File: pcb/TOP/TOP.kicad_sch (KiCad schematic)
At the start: 93 parts, among them J1 Conn_01x04, U1 ICL7660, U2 L78L15_SOT89, U3 TL074, U4 OPA2604

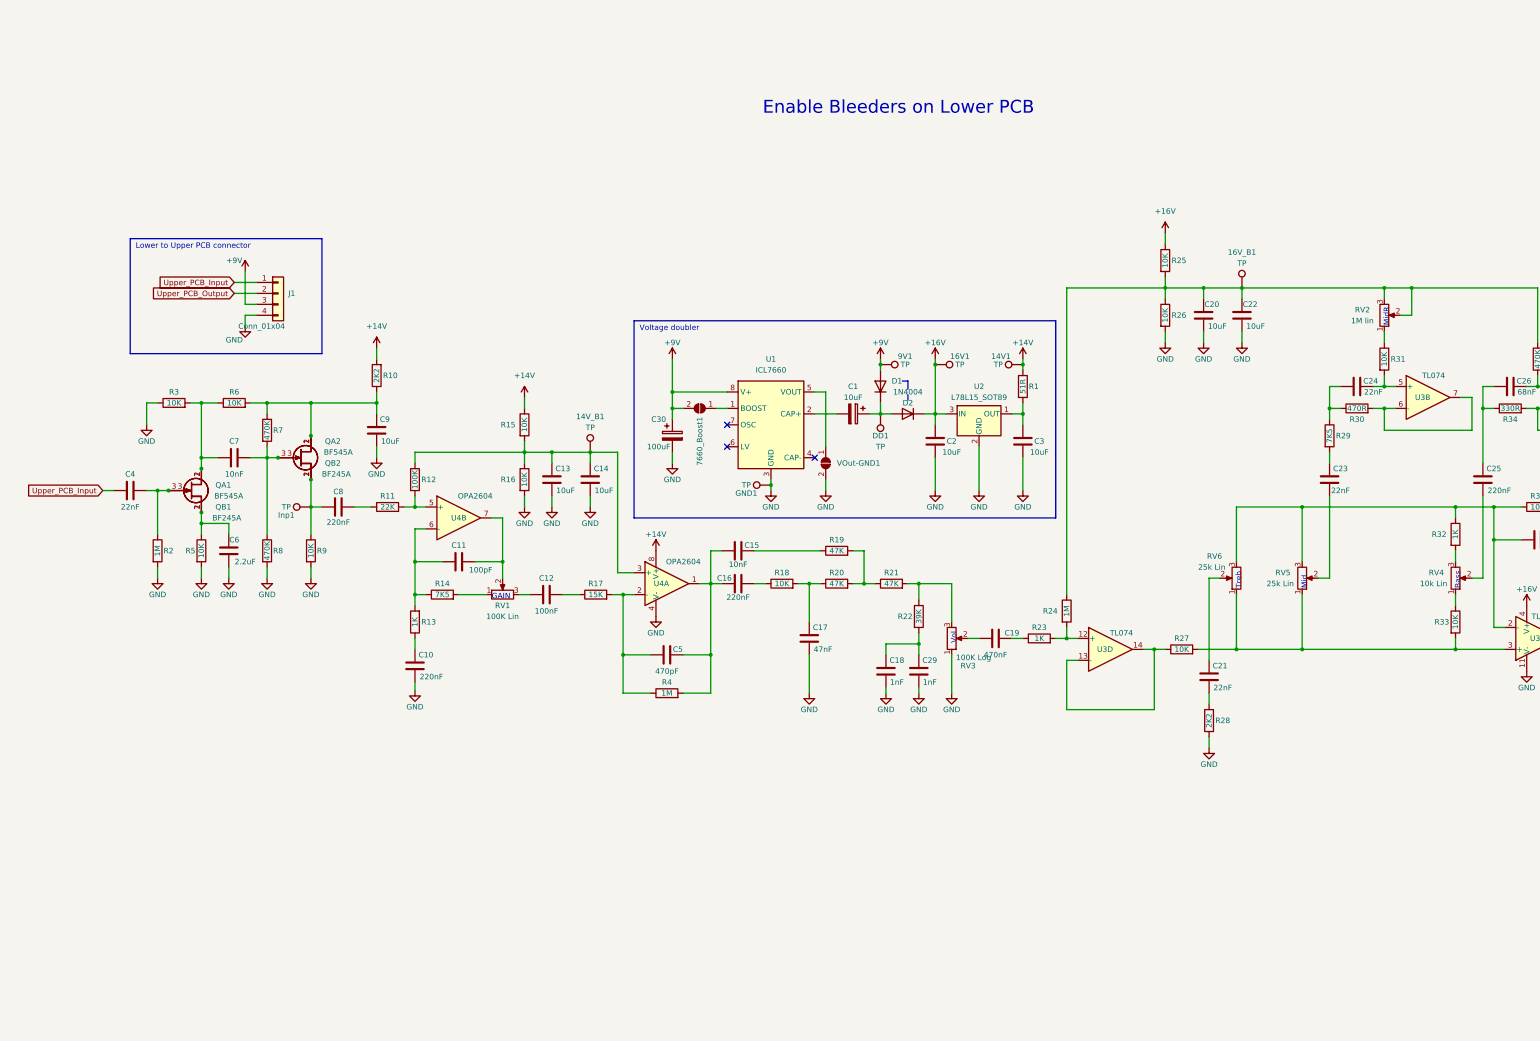
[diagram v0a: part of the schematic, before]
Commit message: [TOP] Fix 7660 -> 7660S in schematic; Make circuit fit for simulation of input stage
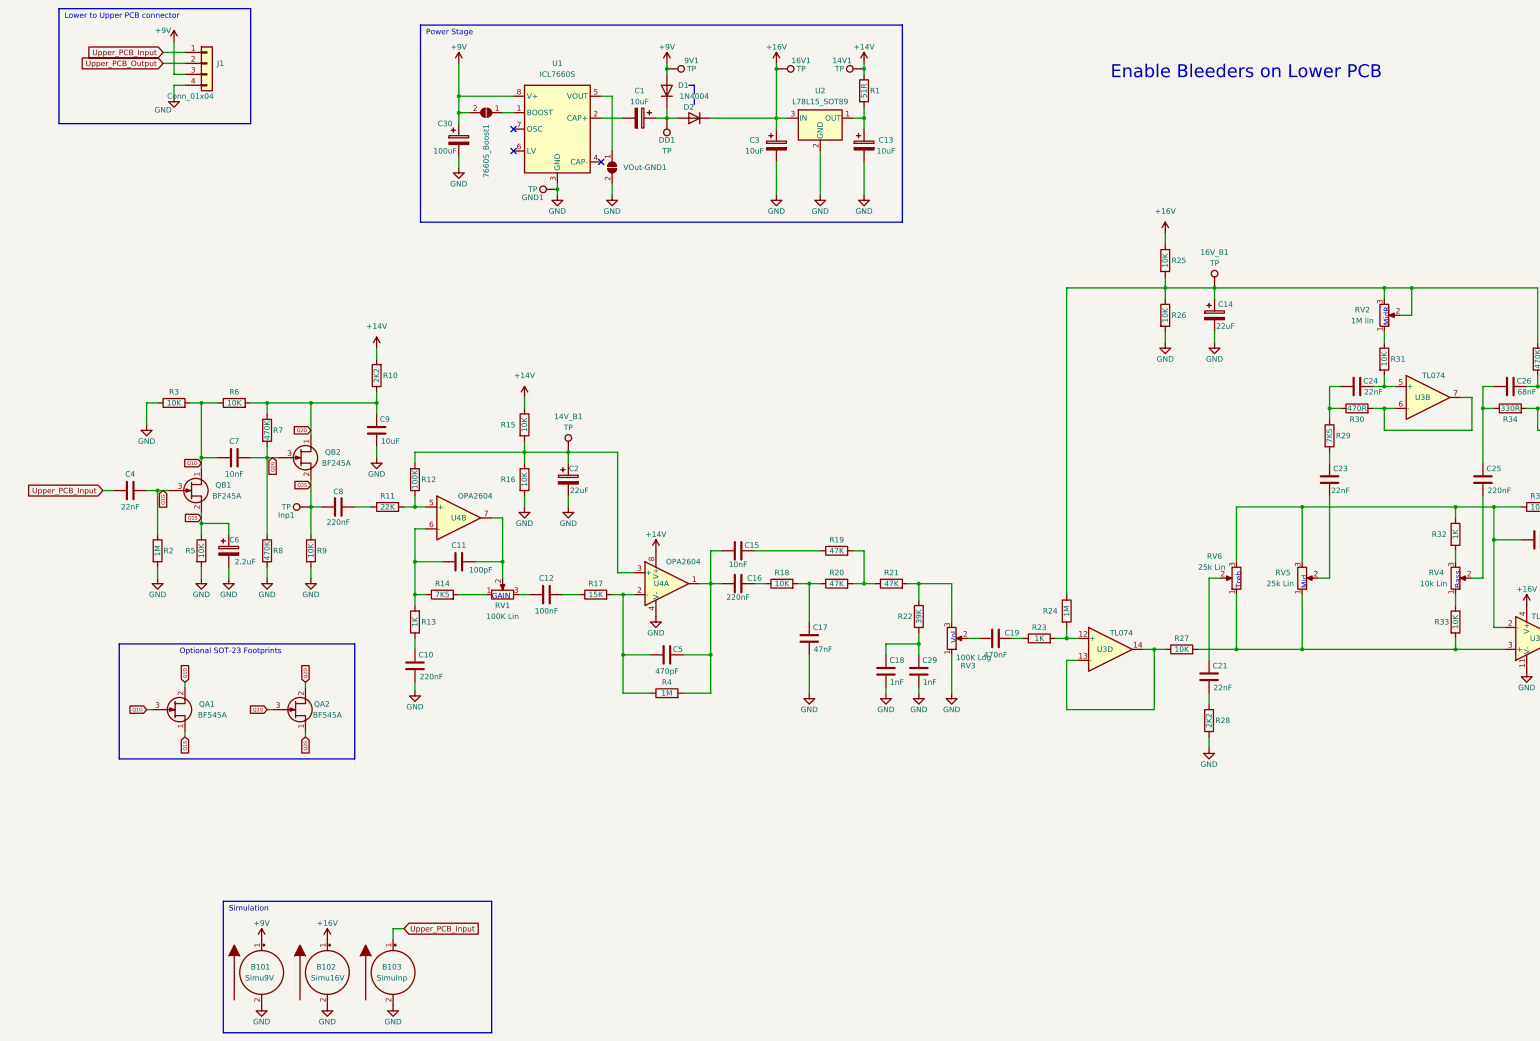
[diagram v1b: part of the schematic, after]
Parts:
- removed C13, C14, C2, C20, C22, C3: 10uF, Capacitor_SMD:C_0805_2012Metric, symbol Device:C
- removed C6: 2.2uF, Capacitor_SMD:C_0603_1608Metric, symbol Device:C
- added B101: Simu9V, symbol pspice:BSOURCE
- added B102: Simu16V, symbol pspice:BSOURCE
- added B103: SimuInp, symbol pspice:BSOURCE
- added C13, C3: 10uF, Capacitor_SMD:CP_Elec_4x5.4, symbol Device:C_Polarized
- added C14, C2: 22uF, symbol Device:C_Polarized
- added C6: 2.2uF, symbol Device:C_Polarized
- 14V1, 14V_B1, 16V1, 16V_B1, 9V1, DD1, GND1, Inp1, J1, RV1, RV2, RV3, RV4, RV5, RV6, U4, VOut-GND1: Spice_Netlist_Enabled (none) -> N
- 7660S_Boost1: renamed from 7660_Boost1; Spice_Netlist_Enabled (none) -> N
- C1, C9: Spice_Model (none) -> 10u; Spice_Netlist_Enabled (none) -> Y; Spice_Primitive (none) -> C
- C10, C16, C25, C8: Spice_Model (none) -> 220n; Spice_Netlist_Enabled (none) -> Y; Spice_Primitive (none) -> C
- C11: Spice_Model (none) -> 100p; Spice_Netlist_Enabled (none) -> Y; Spice_Primitive (none) -> C
- C12: Spice_Model (none) -> 100n; Spice_Netlist_Enabled (none) -> Y; Spice_Primitive (none) -> C
- C15, C7: Spice_Model (none) -> 10n; Spice_Netlist_Enabled (none) -> Y; Spice_Primitive (none) -> C
- C17: Spice_Model (none) -> 47n; Spice_Netlist_Enabled (none) -> Y; Spice_Primitive (none) -> C
- C18, C27, C29: Spice_Model (none) -> 1n; Spice_Netlist_Enabled (none) -> Y; Spice_Primitive (none) -> C
- C19, C28: Spice_Model (none) -> 470n; Spice_Netlist_Enabled (none) -> Y; Spice_Primitive (none) -> C
- C21, C23, C24, C4: Spice_Model (none) -> 22n; Spice_Netlist_Enabled (none) -> Y; Spice_Primitive (none) -> C
- C26: Spice_Model (none) -> 68n; Spice_Netlist_Enabled (none) -> Y; Spice_Primitive (none) -> C
- C30: Spice_Model (none) -> 100u; Spice_Netlist_Enabled (none) -> Y; Spice_Primitive (none) -> C
- C5: Spice_Model (none) -> 470p; Spice_Netlist_Enabled (none) -> Y; Spice_Primitive (none) -> C
- D1, D2: Spice_Lib_File (none) -> /home/chrismettal/mnt/Raidstone/Projects/_KiCAD_libraries_/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; Spice_Model (none) -> D1N4001; Spice_Netlist_Enabled (none) -> Y; Spice_Primitive (none) -> D
- QA1, QA2: Spice_Model (none) -> BF545A; Spice_Netlist_Enabled (none) -> N; Spice_Primitive (none) -> Q
- QB1, QB2: Spice_Lib_File (none) -> /home/chrismettal/mnt/Raidstone/Projects/_KiCAD_libraries_/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; Spice_Model (none) -> BF245A; Spice_Netlist_Enabled (none) -> Y; Spice_Node_Sequence (none) -> 1 3 2; Spice_Primitive (none) -> J
- R1: Spice_Model (none) -> 51; Spice_Netlist_Enabled (none) -> Y; Spice_Primitive (none) -> R
- R10, R28: Spice_Model (none) -> 2.2k; Spice_Netlist_Enabled (none) -> Y; Spice_Primitive (none) -> R
- R11: Spice_Model (none) -> 22k; Spice_Netlist_Enabled (none) -> Y; Spice_Primitive (none) -> R
- R12: Spice_Model (none) -> 100k; Spice_Netlist_Enabled (none) -> Y; Spice_Primitive (none) -> R
- R13, R23, R32: Spice_Model (none) -> 1k; Spice_Netlist_Enabled (none) -> Y; Spice_Primitive (none) -> R
- R14, R29: Spice_Model (none) -> 7.5k; Spice_Netlist_Enabled (none) -> Y; Spice_Primitive (none) -> R
- R15, R16, R18, R25, R26, R27, R3, R31, R33, R36, R5, R6, R9: Spice_Model (none) -> 10k; Spice_Netlist_Enabled (none) -> Y; Spice_Primitive (none) -> R
- R17: Spice_Model (none) -> 15k; Spice_Netlist_Enabled (none) -> Y; Spice_Primitive (none) -> R
- R19, R20, R21: Spice_Model (none) -> 47k; Spice_Netlist_Enabled (none) -> Y; Spice_Primitive (none) -> R
- R2, R24, R4: Spice_Model (none) -> 1meg; Spice_Netlist_Enabled (none) -> Y; Spice_Primitive (none) -> R
- R22: Spice_Model (none) -> 39k; Spice_Netlist_Enabled (none) -> Y; Spice_Primitive (none) -> R
- R30: Spice_Model (none) -> 470; Spice_Netlist_Enabled (none) -> Y; Spice_Primitive (none) -> R
- R34: Spice_Model (none) -> 330; Spice_Netlist_Enabled (none) -> Y; Spice_Primitive (none) -> R
- R35, R7, R8: Spice_Model (none) -> 470k; Spice_Netlist_Enabled (none) -> Y; Spice_Primitive (none) -> R
- U1: value ICL7660 -> ICL7660S; LCSC C356724 -> C357815; Spice_Netlist_Enabled (none) -> N; Spice_Primitive (none) -> R
- U2: Spice_Lib_File (none) -> /home/chrismettal/mnt/Raidstone/Projects/_KiCAD_libraries_/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; Spice_Model (none) -> LM7815C; Spice_Netlist_Enabled (none) -> Y; Spice_Node_Sequence (none) -> 3 1 2; Spice_Primitive (none) -> X
- U3: Spice_Netlist_Enabled (none) -> N; Spice_Primitive (none) -> R
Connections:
- net +16V: now also B102.1 (N+), C3.1
- net +9V: now also B101.1 (N+)
- net GND: now also B101.2 (N-), B102.2 (N-), B103.2 (N-), C13.2, C14.2, C2.2, C3.2, C6.2
- net Upper_PCB_Input: now also B103.1 (N+)
- net at 16V_B1.1, R24.1, R25.2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: now also C14.1
- net Q2D: now reaches C9.1, QA2.2 (D), QB2.1 (D), R10.1, R6.2, R7.1
- net Q2G: now reaches C7.1, QA2.3 (G), QB2.3 (G), R7.2, R8.1
- net at 14V_B1.1, R12.1, R15.2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: now also C2.1
- net Q2S: now reaches C8.2, Inp1.1, QA2.1 (S), QB2.2 (S), R9.1
- net Q1D: now reaches C7.2, QA1.2 (D), QB1.1 (D), R3.2, R6.1
- net Q1S: now reaches QA1.1 (S), QB1.2 (S), R5.1
- net Q1S: now also C6.1
- net Q1G: now reaches C4.1, QA1.3 (G), QB1.3 (G), R2.1
- net at R1.2, U2.1 (OUT): now also C13.1
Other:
- note added: "Optional SOT-23 Footprints"
- note added: "Power Stage"
- note added: "Simulation"
- note removed: "Voltage doubler"
- moved on the sheet: 14V1, 14V_B1, 16V1, 16V_B1, 7660S_Boost1, 9V1, C1, C30, D1, DD1, GND1, J1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

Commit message: [TOP] Update simulation parameters
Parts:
- removed C9: 10uF, Capacitor_SMD:C_0805_2012Metric, symbol Device:C
- added C?: 10uF, symbol Device:C_Polarized
- B102: value Simu16V -> Simu14V; Spice_Model dc 16 pulse(16 16 0 0 0 100) -> dc 14 pulse(14 14 0 0 0 100)
- U2: Spice_Netlist_Enabled Y -> N
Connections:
- net +14V: now also B102.1 (N+)
- net +16V: no longer B102.1 (N+)
- net GND: now also C?.2
- net Q2D: now also C?.1
- net Upper_PCB_Input: no longer C4.2
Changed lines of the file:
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@@
     )
   )
-  (global_label "Upper_PCB_Input" (shape input) (at 31.75 142.24 180) (fields_autoplaced)
+  (global_label "Upper_PCB_Input" (shape input) (at 30.48 142.24 180) (fields_autoplaced)
     (effects (font (size 1.27 1.27)) (justify right))
-    (property "Intersheet References" "${INTERSHEET_REFS}" (id 0) (at 13.3107 142.1606 0)
+    (property "Intersheet References" "${INTERSHEET_REFS}" (id 0) (at 12.0407 142.1606 0)
       (effects (font (size 1.27 1.27)) (justify right) hide)
     )
@@
       (effects (font (size 1.27 1.27)) hide)
     )
-    (property "Spice_Netlist_Enabled" "Y" (id 7) (at 198.12 55.88 0)
+    (property "Spice_Netlist_Enabled" "N" (id 7) (at 198.12 55.88 0)
       (effects (font (size 1.27 1.27)) hide)
     )
@@
       (effects (font (size 1.27 1.27)) (justify left))
     )
-    (property "Value" "Simu16V" (id 1) (at 80.01 255.27 0)
+    (property "Value" "Simu14V" (id 1) (at 80.01 255.27 0)
       (effects (font (size 1.27 1.27)) (justify left))
     )
@@
       (effects (font (size 1.27 1.27)) hide)
     )
-    (property "Spice_Model" "dc 16 pulse(16 16 0 0 0 100)" (id 5) (at 83.82 254 0)
+    (property "Spice_Model" "dc 14 pulse(14 14 0 0 0 100)" (id 5) (at 83.82 254 0)
       (effects (font (size 1.27 1.27)) hide)
     )
@@
     (pin "2")
   )
-  (symbol (lib_name "+16V_1") (lib_id "MeineBibli:+16V") (at 83.82 246.38 0) (unit 1)
-    (in_bom yes) (on_board yes)
-    (property "Reference" "#PWR?" (id 0) (at 83.82 250.19 0)
-      (effects (font (size 1.27 1.27)) hide)
-    )
-    (property "Value" "+16V" (id 1) (at 83.82 242.57 0))
-    (property "Footprint" "" (id 2) (at 83.82 246.38 0)
-      (effects (font (size 1.27 1.27)) hide)
-    )
-    (property "Datasheet" "" (id 3) (at 83.82 246.38 0)
-      (effects (font (size 1.27 1.27)) hide)
-    )
-    (pin "1")
-  )
   (symbol (lib_id "Device:C") (at 381 176.53 270) (unit 1)
     (in_bom yes) (on_board yes)
@@
     (pin "1")
   )
-  (symbol (lib_id "Device:C") (at 95.25 128.27 0) (unit 1)
-    (in_bom yes) (on_board yes)
-    (property "Reference" "C9" (id 0) (at 97.155 125.73 0))
-    (property "Value" "10uF" (id 1) (at 98.425 130.81 0))
-    (property "Footprint" "Capacitor_SMD:C_0805_2012Metric" (id 2) (at 96.2152 132.08 0)
-      (effects (font (size 1.27 1.27)) hide)
-    )
-    (property "Datasheet" "" (id 3) (at 95.25 128.27 0)
-      (effects (font (size 1.27 1.27)) hide)
-    )
-    (property "LCSC" "C15850" (id 4) (at 95.25 128.27 0)
-      (effects (font (size 1.27 1.27)) hide)
-    )
-    (property "Spice_Model" "10u" (id 5) (at 95.25 128.27 0)
-      (effects (font (size 1.27 1.27)) hide)
-    )
-    (property "Spice_Netlist_Enabled" "Y" (id 6) (at 95.25 128.27 0)
-      (effects (font (size 1.27 1.27)) hide)
-    )
-    (property "Spice_Primitive" "C" (id 7) (at 95.25 128.27 0)
-      (effects (font (size 1.27 1.27)) hide)
-    )
-    (pin "1")
-    (pin "2")
-  )
   (symbol (lib_id "power:GND") (at 149.86 73.66 0) (unit 1)
     (in_bom yes) (on_board yes)
@@
     (pin "2")
   )
+  (symbol (lib_id "Device:C_Polarized") (at 95.25 128.27 0) (unit 1)
+    (in_bom yes) (on_board yes)
+    (property "Reference" "C?" (id 0) (at 96.52 125.73 0))
+    (property "Value" "10uF" (id 1) (at 97.79 130.81 0))
+    (property "Footprint" "" (id 2) (at 96.2152 132.08 0)
+      (effects (font (size 1.27 1.27)) hide)
+    )
+    (property "Datasheet" "" (id 3) (at 95.25 128.27 0)
+      (effects (font (size 1.27 1.27)) hide)
+    )
+    (property "LCSC" "" (id 4) (at 95.25 128.27 0)
+      (effects (font (size 1.27 1.27)) hide)
+    )
+    (property "Spice_Model" "10u" (id 5) (at 95.25 128.27 0)
+      (effects (font (size 1.27 1.27)) hide)
+    )
+    (property "Spice_Netlist_Enabled" "Y" (id 6) (at 95.25 128.27 0)
+      (effects (font (size 1.27 1.27)) hide)
+    )
+    (property "Spice_Primitive" "C" (id 7) (at 95.25 128.27 0)
+      (effects (font (size 1.27 1.27)) hide)
+    )
+    (pin "1")
+    (pin "2")
+  )
   (symbol (lib_id "power:GND") (at 80.01 162.56 0) (unit 1)
     (in_bom yes) (on_board yes)
@@
     (pin "2")
   )
+  (symbol (lib_id "MeineBibli:+14V") (at 83.82 246.38 0) (unit 1)
+    (in_bom yes) (on_board yes)
+    (property "Reference" "#PWR?" (id 0) (at 83.82 250.19 0)
+      (effects (font (size 1.27 1.27)) hide)
+    )
+    (property "Value" "+14V" (id 1) (at 83.82 242.57 0))
+    (property "Footprint" "" (id 2) (at 83.82 246.38 0)
+      (effects (font (size 1.27 1.27)) hide)
+    )
+    (property "Datasheet" "" (id 3) (at 83.82 246.38 0)
+      (effects (font (size 1.27 1.27)) hide)
+    )
+    (pin "1")
+  )
   (symbol (lib_id "Device:C_Polarized") (at 139.7 139.7 0) (unit 1)
     (in_bom yes) (on_board yes)
@@
       (reference "#PWR?") (unit 1) (value "GND") (footprint "")
     )
-    (path "/65424e95-5fd5-4975-8acc-3bfda5f68382"
-      (reference "#PWR?") (unit 1) (value "+16V") (footprint "")
-    )
     (path "/77736f92-0ab3-4583-8c75-6bd1a6de3469"
       (reference "#PWR?") (unit 1) (value "+9V") (footprint "")
@@
       (reference "#PWR?") (unit 1) (value "GND") (footprint "")
     )
+    (path "/e7a1e26f-5035-4e36-9270-3d10535fba04"
+      (reference "#PWR?") (unit 1) (value "+14V") (footprint "")
+    )
     (path "/16343701-80cb-4ddd-be03-e72f0ff5bc43"
       (reference "9V1") (unit 1) (value "TP") (footprint "TestPoint:TestPoint_Pad_D2.0mm")
@@
     )
     (path "/650bea18-a494-4622-8130-de20719cf431"
-      (reference "B102") (unit 1) (value "Simu16V") (footprint "")
+      (reference "B102") (unit 1) (value "Simu14V") (footprint "")
     )
     (path "/cf8f8131-0e49-4d9f-a19a-3559fee0ad2c"
@@
       (reference "C8") (unit 1) (value "220nF") (footprint "Capacitor_SMD:C_0603_1608Metric")
     )
-    (path "/c06a5ba9-163c-4d19-97c1-31a99e85433a"
-      (reference "C9") (unit 1) (value "10uF") (footprint "Capacitor_SMD:C_0805_2012Metric")
-    )
     (path "/98e5ae60-2476-4488-acb7-6774d7a2639c"
       (reference "C10") (unit 1) (value "220nF") (footprint "Capacitor_SMD:C_0603_1608Metric")
@@
       (reference "C30") (unit 1) (value "100uF") (footprint "Capacitor_SMD:CP_Elec_6.3x5.4_Nichicon")
     )
+    (path "/c4de825c-cba7-4401-9cb0-eacc4fd9b81d"
+      (reference "C?") (unit 1) (value "10uF") (footprint "")
+    )
     (path "/0ff4343c-407d-4c6b-92a4-beb371940202"
